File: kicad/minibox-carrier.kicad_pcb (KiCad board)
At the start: 4 copper layers, 100 x 112 mm, 14 parts, among them J1 ESP32-S3 LEFT - USB AT TOP, J11 THREE-KEY CABLE KeyA KeyB Key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, J12 JOYSTICK CABLE G V X Y K, J2 ESP32-S3 RIGHT - USB AT TOP, J3 INMP441 2x3 VDD GND / SCK WS 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, J4 MAX98357A LRC BCLK DIN GAIN S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, J5 PCF8563T CLK INT SDA SCL VCC 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, J6 ST7796 14-PIN DISPLAY HEADER, J7 5.08mm wire terminal, J8 5.08mm wire terminal

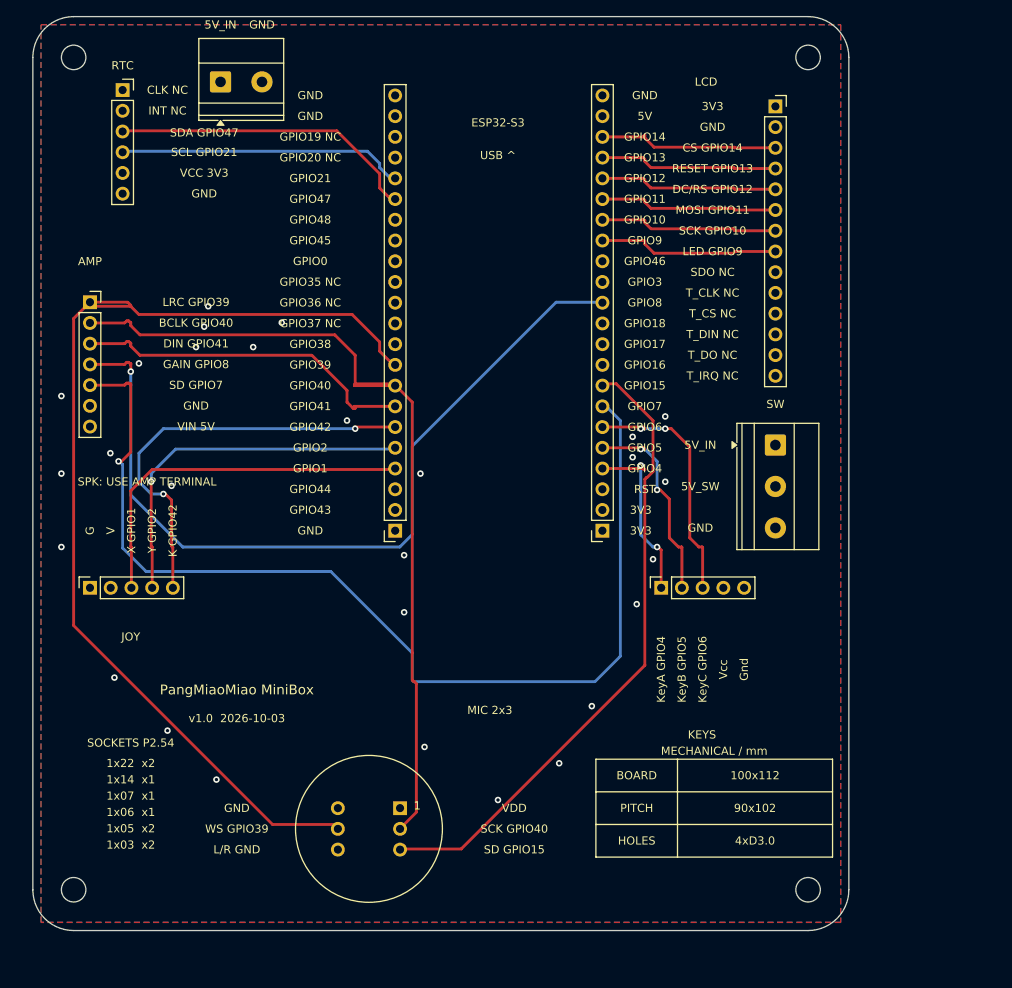
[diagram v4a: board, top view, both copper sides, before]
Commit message: Redesign Minibox carrier layout and synchronize firmware
Add four directly soldered keyboard switches, the exact joystick footprint, and Type-C CC pull-downs. Release GPIO42 and synchronize wiring and firmware. Include part references, renders, and engineering-review fabrication and assembly deliverables; production approval remains pending.

Co-authored-by: Copilot App <223556219+Copilot@users.noreply.github.com>
Copilot-Session: e98879a8-1dff-48d4-a7f7-1d056a166875
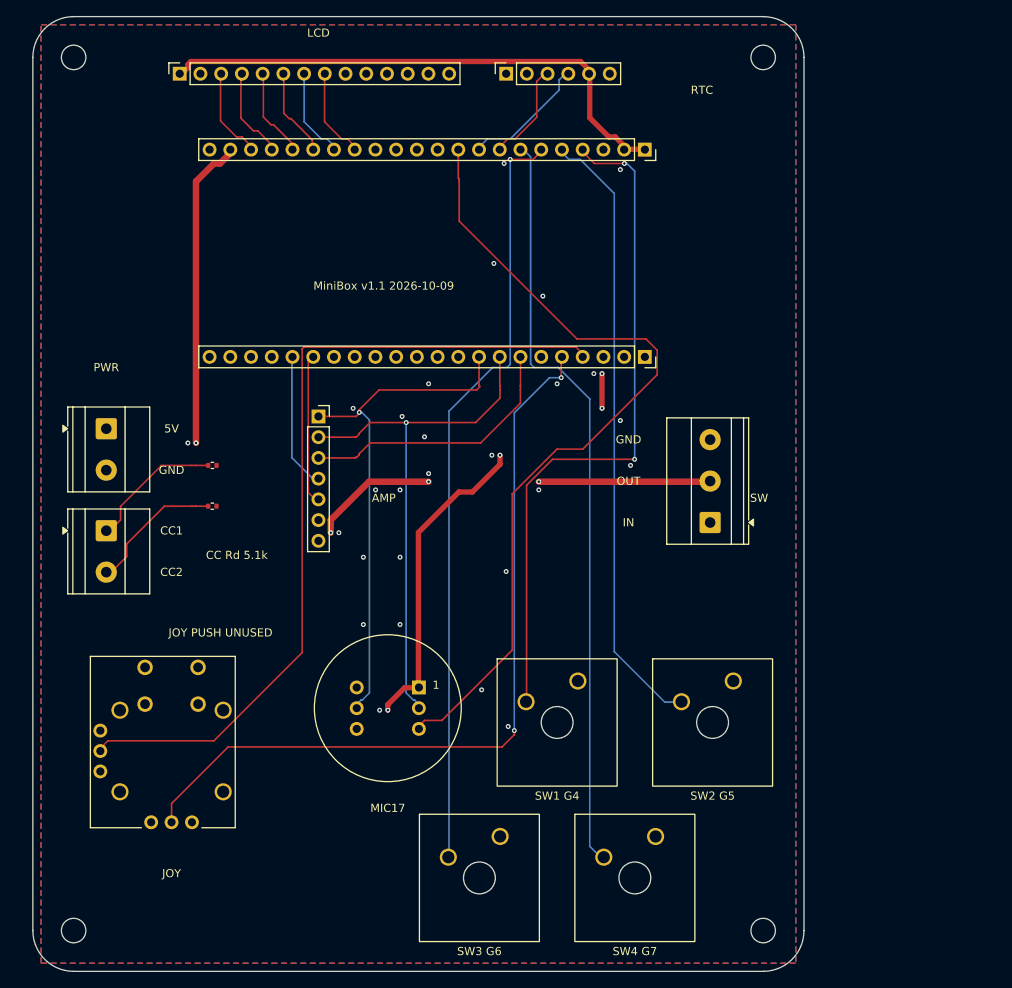
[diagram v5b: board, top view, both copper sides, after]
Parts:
- removed J11: THREE-KEY CABLE KeyA KeyB KeyC Vcc Gnd, Connector_PinSocket_2.54mm:PinSocket_1x05_P2.54mm_Vertical
- removed J12: JOYSTICK CABLE G V X Y K, Connector_PinSocket_2.54mm:PinSocket_1x05_P2.54mm_Vertical
- added J9: 5.08mm wire terminal, TerminalBlock_Phoenix:TerminalBlock_Phoenix_MKDS-1,5-2-5.08_1x02_P5.08mm_Horizontal, F.Cu at (14.0, 66.0)
- added JS1: YV13S-L7.85-B10Ka(60)-0-DL01, Minibox:YV13S_L7.85_B10Ka_60_0_DL01, F.Cu at (22.0, 93.0)
- added R1: 5.1k 1%, Resistor_SMD:R_0402_1005Metric, F.Cu at (27.0, 58.0)
- added R2: 5.1k 1%, Resistor_SMD:R_0402_1005Metric, F.Cu at (27.0, 63.0)
- added SW1: CPG151101D13, Minibox:CPG151101D13, F.Cu at (69.2, 89.5)
- added SW2: CPG151101D13, Minibox:CPG151101D13, F.Cu at (88.3, 89.5)
- added SW3: CPG151101D13, Minibox:CPG151101D13, F.Cu at (59.7, 108.5)
- added SW4: CPG151101D13, Minibox:CPG151101D13, F.Cu at (78.8, 108.5)
- H1, H2, H3, H4: value MountingHole_3mm -> M3 NPTH
- J1: value ESP32-S3 LEFT - USB AT TOP -> ESP32-S3 J1 - USB LEFT
- J2: value ESP32-S3 RIGHT - USB AT TOP -> ESP32-S3 J3 - USB LEFT
- J3: value INMP441 2x3 VDD GND / SCK WS / SD LR -> INMP441 two 1x3 sockets
- J4: value MAX98357A LRC BCLK DIN GAIN SD GND VIN -> MAX98357A module socket
- J5: value PCF8563T CLK INT SDA SCL VCC GND -> PCF8563T upright module
- J6: value ST7796 14-PIN DISPLAY HEADER -> ST7796 14-pin display
- moved J6 73.1 mm to (23.0, 10.0), turned to 90 degrees
- moved J5 47.0 mm to (63.0, 10.0), turned to 90 degrees
- moved J1 47.0 mm to (80.0, 19.3), turned to -90 degrees
- moved J8 44.7 mm to (14.0, 53.5), turned to -90 degrees
- moved J2 37.3 mm to (80.0, 44.7), turned to -90 degrees
- moved J4 31.3 mm to (40.0, 52.0)
- moved J3 15.0 mm to (52.3, 85.2)
- moved J7 12.4 mm to (88.0, 65.0), turned to 90 degrees
- moved H4 7.43 mm to (94.5, 115.0)
- moved H2 5.50 mm to (94.5, 8.00)
- moved H3 5.00 mm to (10.0, 115.0)
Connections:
- J1 pad 10: GPIO17 -> MIC_SD
- J1 pad 11: GPIO18 -> (no net)
- J1 pad 12: AMP_GAIN -> (no net)
- J1 pad 13: GPIO3 -> (no net)
- J1 pad 14: GPIO46 -> (no net)
- J1 pad 7: AMP_SD -> BUTTON4
- J1 pad 8: MIC_SD -> RTC_SDA
- J1 pad 9: GPIO16 -> RTC_SCL
- J2 pad 10: GPIO38 -> (no net)
- J2 pad 14: GPIO0 -> (no net)
- J2 pad 15: GPIO45 -> (no net)
- J2 pad 16: GPIO48 -> (no net)
- J2 pad 17: RTC_SDA -> AMP_SD
- J2 pad 18: RTC_SCL -> AMP_GAIN
- J2 pad 2: GPIO43 -> (no net)
- J2 pad 3: GPIO44 -> (no net)
- J2 pad 6: GPIO42 -> (no net)
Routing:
- net AMP_SD: track 129.4 -> 18.7 mm, vias 1 -> 0
- net BUTTON4: track 0.00 -> 93.3 mm
- net AMP_GAIN: track 101.1 -> 16.7 mm, vias 1 -> 0
- net I2S_WS: track 129.8 -> 62.9 mm, vias 0 -> 1
- net BUTTON3: track 30.9 -> 94.3 mm, vias 2 -> 1
- net BUTTON1: track 22.4 -> 84.3 mm
- net GPIO1: track 45.7 -> 102.6 mm
- net GPIO42: track 52.2 -> 0.00 mm, vias 2 -> 0
- net GPIO2: track 45.5 -> 97.4 mm, vias 1 -> 2
- net RECORD: track 25.6 -> 76.0 mm, vias 2 -> 0
- net I2S_BCLK: track 105.0 -> 65.1 mm, vias 0 -> 1
- net 3V3: track 242.1 -> 204.9 mm, vias 0 -> 4
- net 5V_SW: track 148.9 -> 112.1 mm, vias 0 -> 4
- net RTC_SDA: track 38.3 -> 12.5 mm
- net MIC_SD: track 78.0 -> 101.3 mm
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- added copper zone on In2.Cu, net GND
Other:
- board size 100 x 112 mm -> 94.5 x 117 mm
- rule pad_to_mask_clearance: 0.05 -> 0.02
- board text added: "ANTENNA: NO COPPER / NO MODULES"
- board text added: "BCLK G40"
- board text added: "BCLK40"
- board text added: "BL"
- board text added: "BL G9"
- board text added: "CC Rd 5.1k"
- board text added: "CC1"
- board text added: "CC2"
- board text added: "CS"
- board text added: "CS G14"
- board text added: "DC"
- board text added: "DC G12"
- board text added: "DIN G41"
- board text added: "DIN41"
- board text added: "ESP32 USB <"
- board text added: "G0 NC"
- board text added: "G18 NC"
- board text added: "G3 NC"
- board text added: "G35 NC"
- board text added: "G36 NC"
- board text added: "G37 NC"
- board text added: "G38 NC"
- board text added: "G42 NC"
- board text added: "G45 NC"
- board text added: "G46 NC"
- board text added: "G48 NC"
- board text added: "G8 NC"
- board text added: "GAIN G21"
- board text added: "GAIN21"
- board text added: "IN"
- board text added: "JOY PUSH UNUSED"
- board text added: "JOYSTICK MOTION D30"
- board text added: "KEY1 G4"
- board text added: "KEY2 G5"
- board text added: "KEY3 G6"
- board text added: "KEY4 G7"
- board text added: "KEYCAP MAX 18x18"
- board text added: "MAX98357 MODULE RESERVATION"
- board text added: "MIC G17"
- board text added: "MIC17"
- board text added: "MODULES ABOVE / CONTROLS BELOW"
- board text added: "MOSI"
- board text added: "MOSI G11"
- board text added: "MiniBox v1.1 2026-10-09"
- board text added: "NC"
- board text added: "OUT"
- board text added: "PWR"
- board text added: "RST G13"
- board text added: "RST NC"
- board text added: "RTC + BATTERY: MAX 12mm THICK"
- board text added: "RX NC"
- board text added: "SCK"
- board text added: "SCK G10"
- board text added: "SCL G16"
- board text added: "SCL16"
- board text added: "SD G47"
- board text added: "SD47"
- board text added: "SDA G15"
- board text added: "SDA15"
- board text added: "SW1 G4"
- board text added: "SW2 G5"
- board text added: "SW3 G6"
- board text added: "SW4 G7"
- board text added: "TX NC"
- board text added: "USB+ NC"
- board text added: "USB- NC"
- board text added: "WS G39"
- board text added: "WS39"
- board text added: "X G1"
- board text added: "Y G2"
- board text removed: "100x112"
- board text removed: "1x03 x2"
- board text removed: "1x05 x2"
- board text removed: "1x06 x1"
- board text removed: "1x07 x1"
- board text removed: "1x14 x1"
- board text removed: "1x22 x2"
- board text removed: "4xD3.0"
- board text removed: "5V_IN"
- board text removed: "5V_SW"
- board text removed: "90x102"
- board text removed: "BCLK GPIO40"
- board text removed: "BOARD"
- board text removed: "CS GPIO14"
- board text removed: "DC/RS GPIO12"
- board text removed: "DIN GPIO41"
- board text removed: "ESP32-S3"
- board text removed: "G"
- board text removed: "GAIN GPIO8"
- board text removed: "GPIO0"
- board text removed: "GPIO1"
- board text removed: "GPIO10"
- board text removed: "GPIO11"
- board text removed: "GPIO12"
- board text removed: "GPIO13"
- board text removed: "GPIO14"
- board text removed: "GPIO15"
- board text removed: "GPIO16"
- board text removed: "GPIO17"
- board text removed: "GPIO18"
- board text removed: "GPIO19 NC"
- board text removed: "GPIO2"
- board text removed: "GPIO20 NC"
- board text removed: "GPIO21"
- board text removed: "GPIO3"
- board text removed: "GPIO35 NC"
- board text removed: "GPIO36 NC"
- board text removed: "GPIO37 NC"
- board text removed: "GPIO38"
- board text removed: "GPIO39"
- board text removed: "GPIO4"
- board text removed: "GPIO40"
- board text removed: "GPIO41"
- board text removed: "GPIO42"
- board text removed: "GPIO43"
- board text removed: "GPIO44"
- board text removed: "GPIO45"
- board text removed: "GPIO46"
- board text removed: "GPIO47"
- board text removed: "GPIO48"
- board text removed: "GPIO5"
- board text removed: "GPIO6"
- board text removed: "GPIO7"
- board text removed: "GPIO8"
- board text removed: "GPIO9"
- board text removed: "Gnd"
- board text removed: "HOLES"
- board text removed: "K GPIO42"
- board text removed: "KEYS"
- board text removed: "KeyA GPIO4"
- board text removed: "KeyB GPIO5"
- board text removed: "KeyC GPIO6"
- board text removed: "L/R GND"
- board text removed: "LED GPIO9"
- board text removed: "LRC GPIO39"
- board text removed: "MECHANICAL / mm"
- board text removed: "MIC 2x3"
- board text removed: "MOSI GPIO11"
- board text removed: "PITCH"
- board text removed: "PangMiaoMiao MiniBox"
- board text removed: "RESET GPIO13"
- board text removed: "SCK GPIO10"
- board text removed: "SCK GPIO40"
- board text removed: "SCL GPIO21"
- board text removed: "SD GPIO15"
- board text removed: "SD GPIO7"
- board text removed: "SDA GPIO47"
- board text removed: "SDO NC"
- board text removed: "SOCKETS P2.54"
- board text removed: "SPK: USE AMP TERMINAL"
- board text removed: "T_CLK NC"
- board text removed: "T_CS NC"
- board text removed: "T_DIN NC"
- board text removed: "T_DO NC"
- board text removed: "T_IRQ NC"
- board text removed: "USB ^"
- board text removed: "V"
- board text removed: "VCC 3V3"
- board text removed: "VDD"
- board text removed: "VIN 5V"
- board text removed: "Vcc"
- board text removed: "WS GPIO39"
- board text removed: "X GPIO1"
- board text removed: "Y GPIO2"
- board text removed: "v1.0 2026-10-03"

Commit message: Refine carrier layout and remove redundant ground stitching
Update pin silkscreen, swap RTC SDA/SCL to GPIO16/15, refine control placement and pad clearance, retain 23 ground vias, and refresh aligned CAM and engineering-review artifacts.

Co-authored-by: Copilot App <223556219+Copilot@users.noreply.github.com>
Copilot-Session: e98879a8-1dff-48d4-a7f7-1d056a166875
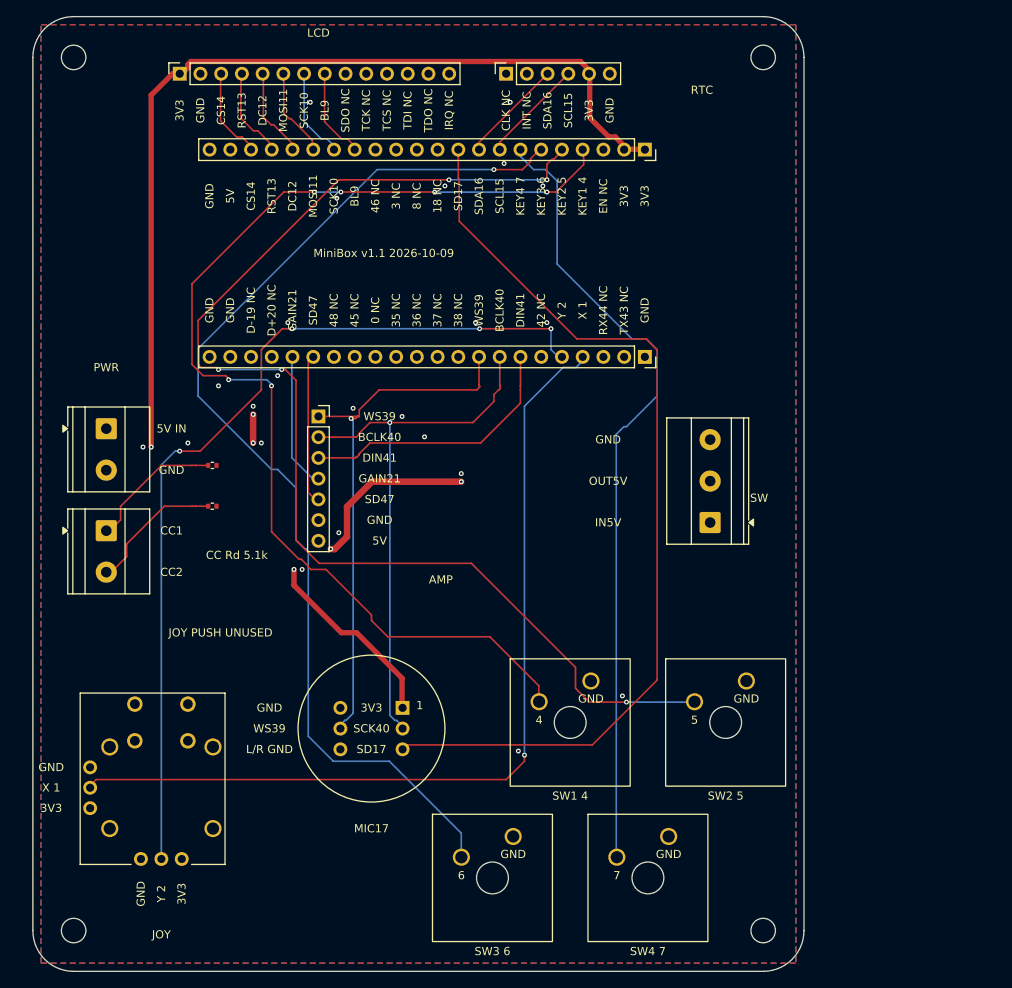
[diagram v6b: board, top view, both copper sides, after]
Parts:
- moved JS1 4.67 mm to (20.8, 97.5)
- moved J3 3.20 mm to (50.3, 87.7)
- moved SW1 1.60 mm to (70.8, 89.5)
- moved SW4 1.60 mm to (80.4, 108.5)
- moved SW2 1.60 mm to (89.9, 89.5)
- moved SW3 1.60 mm to (61.3, 108.5)
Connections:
- J1 pad 8: RTC_SDA -> RTC_SCL
- J1 pad 9: RTC_SCL -> RTC_SDA
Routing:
- net RECORD: track 76.0 -> 151.0 mm, vias 0 -> 5
- net BUTTON1: track 84.3 -> 137.9 mm, vias 2 -> 6
- net BUTTON3: track 94.3 -> 132.7 mm
- net MIC_SD: track 101.3 -> 114.9 mm
- net GPIO2: track 97.4 -> 110.2 mm, vias 2 -> 4
- net 3V3: track 204.9 -> 216.9 mm, vias 4 -> 2
- net GPIO1: track 102.6 -> 108.3 mm, vias 0 -> 1
- net BUTTON4: track 93.3 -> 98.0 mm
- net RTC_SCL: track 15.7 -> 12.8 mm
- net I2S_WS: track 62.9 -> 65.5 mm
- net I2S_BCLK: track 65.1 -> 67.5 mm
- net 5V_SW: track 112.1 -> 113.2 mm
- net GND: vias 27 -> 23
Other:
- board text added: "0 NC"
- board text added: "18 NC"
- board text added: "3 NC"
- board text added: "35 NC"
- board text added: "36 NC"
- board text added: "37 NC"
- board text added: "38 NC"
- board text added: "4"
- board text added: "42 NC"
- board text added: "45 NC"
- board text added: "46 NC"
- board text added: "48 NC"
- board text added: "5"
- board text added: "5V IN"
- board text added: "6"
- board text added: "7"
- board text added: "8 NC"
- board text added: "BL9"
- board text added: "CS14"
- board text added: "D+20 NC"
- board text added: "D-19 NC"
- board text added: "DC12"
- board text added: "EN NC"
- board text added: "IN5V"
- board text added: "IRQ NC"
- board text added: "KEY1 4"
- board text added: "KEY2 5"
- board text added: "KEY3 6"
- board text added: "KEY4 7"
- board text added: "L/R GND"
- board text added: "MOSI11"
- board text added: "OUT5V"
- board text added: "RST13"
- board text added: "RX44 NC"
- board text added: "SCK10"
- board text added: "SCK40"
- board text added: "SCL15"
- board text added: "SD17"
- board text added: "SDA16"
- board text added: "SDO NC"
- board text added: "SW1 4"
- board text added: "SW2 5"
- board text added: "SW3 6"
- board text added: "SW4 7"
- board text added: "TCK NC"
- board text added: "TCS NC"
- board text added: "TDI NC"
- board text added: "TDO NC"
- board text added: "TX43 NC"
- board text added: "X 1"
- board text added: "Y 2"
- board text removed: "BCLK G40"
- board text removed: "BL"
- board text removed: "BL G9"
- board text removed: "CS"
- board text removed: "CS G14"
- board text removed: "DC"
- board text removed: "DC G12"
- board text removed: "DIN G41"
- board text removed: "G0 NC"
- board text removed: "G18 NC"
- board text removed: "G3 NC"
- board text removed: "G35 NC"
- board text removed: "G36 NC"
- board text removed: "G37 NC"
- board text removed: "G38 NC"
- board text removed: "G42 NC"
- board text removed: "G45 NC"
- board text removed: "G46 NC"
- board text removed: "G48 NC"
- board text removed: "G8 NC"
- board text removed: "GAIN G21"
- board text removed: "IN"
- board text removed: "KEY1 G4"
- board text removed: "KEY2 G5"
- board text removed: "KEY3 G6"
- board text removed: "KEY4 G7"
- board text removed: "MIC G17"
- board text removed: "MOSI"
- board text removed: "MOSI G11"
- board text removed: "NC"
- board text removed: "OUT"
- board text removed: "RST"
- board text removed: "RST G13"
- board text removed: "RST NC"
- board text removed: "RX NC"
- board text removed: "SCK"
- board text removed: "SCK G10"
- board text removed: "SCL G16"
- board text removed: "SCL16"
- board text removed: "SD G47"
- board text removed: "SDA G15"
- board text removed: "SDA15"
- board text removed: "SW1 G4"
- board text removed: "SW2 G5"
- board text removed: "SW3 G6"
- board text removed: "SW4 G7"
- board text removed: "TX NC"
- board text removed: "USB+ NC"
- board text removed: "USB- NC"
- board text removed: "WS G39"
- board text removed: "X G1"
- board text removed: "Y G2"

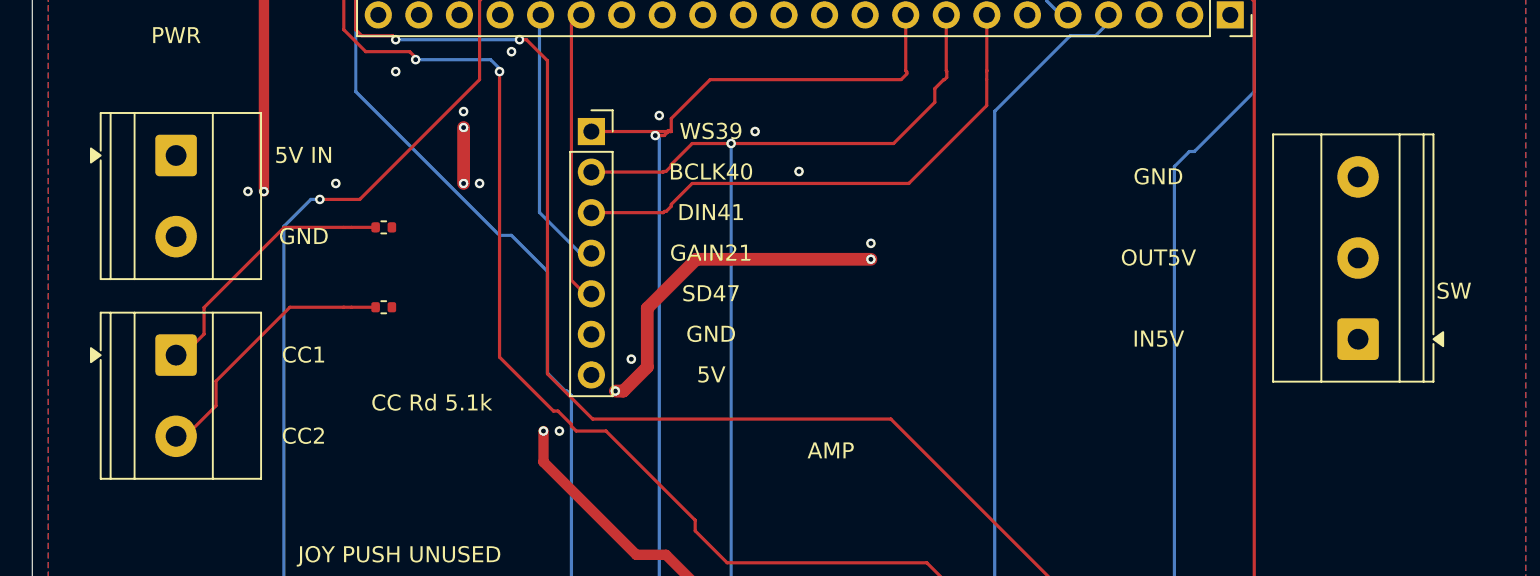
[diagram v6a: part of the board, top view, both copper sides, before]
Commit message: Save carrier sourcing and reproducible JLC placement corrections
Preserve exact part IDs, factory-saved placement readback and datum-aware CPL export. Adapt selected terminal footprints and archive matching manufacturing review files. Document reusable domestic ordering routes and controls separately from board-specific parameters.

Co-authored-by: Copilot App <223556219+Copilot@users.noreply.github.com>

Copilot-Session: e98879a8-1dff-48d4-a7f7-1d056a166875
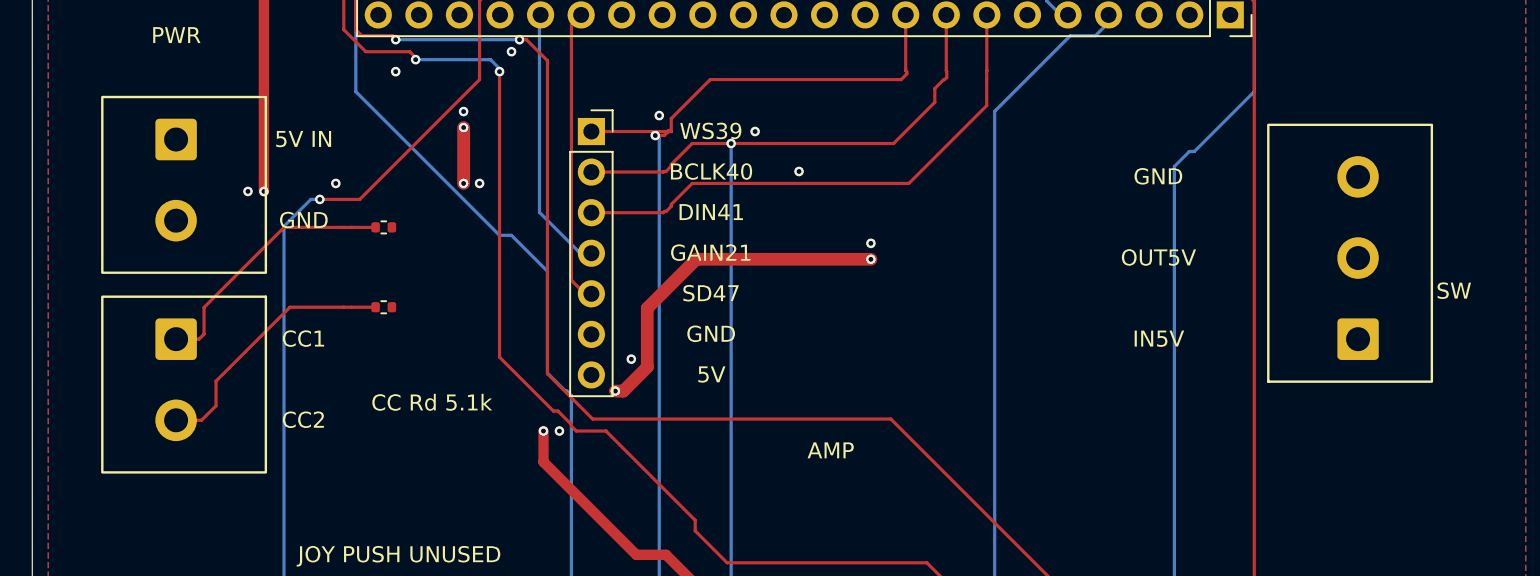
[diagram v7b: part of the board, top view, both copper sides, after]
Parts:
- J7: value 5.08mm wire terminal -> WJ500V-5.08-03P-14-00A; footprint TerminalBlock_Phoenix:TerminalBlock_Phoenix_MKDS-1,5-3-5.08_1x03_P5.08mm_Horizontal -> Minibox:WJ500V_5.08_3P
- J8, J9: value 5.08mm wire terminal -> WJ500V-5.08-2P; footprint TerminalBlock_Phoenix:TerminalBlock_Phoenix_MKDS-1,5-2-5.08_1x02_P5.08mm_Horizontal -> Minibox:WJ500V_5.08_2P
- moved J8 1.00 mm to (14.0, 52.5)
- moved J9 1.00 mm to (14.0, 65.0)
